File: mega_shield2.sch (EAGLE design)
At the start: 36 parts, among them IC1 L298, IC2 LM2937ET-5V, J2 Mega R3

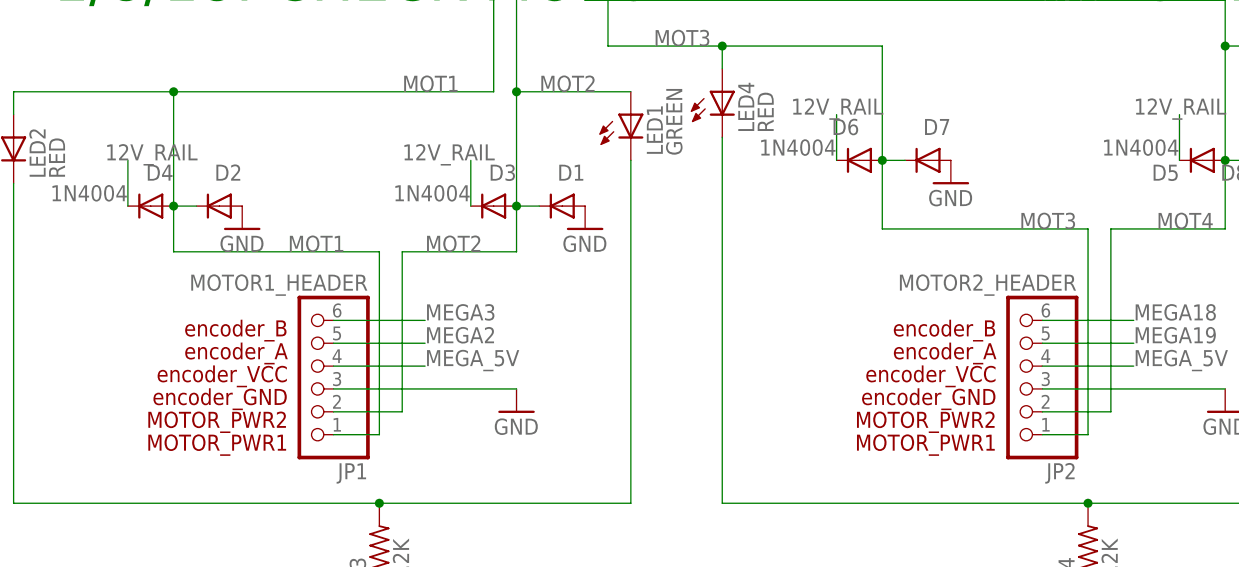
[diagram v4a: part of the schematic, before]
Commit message: changes to silkscreen
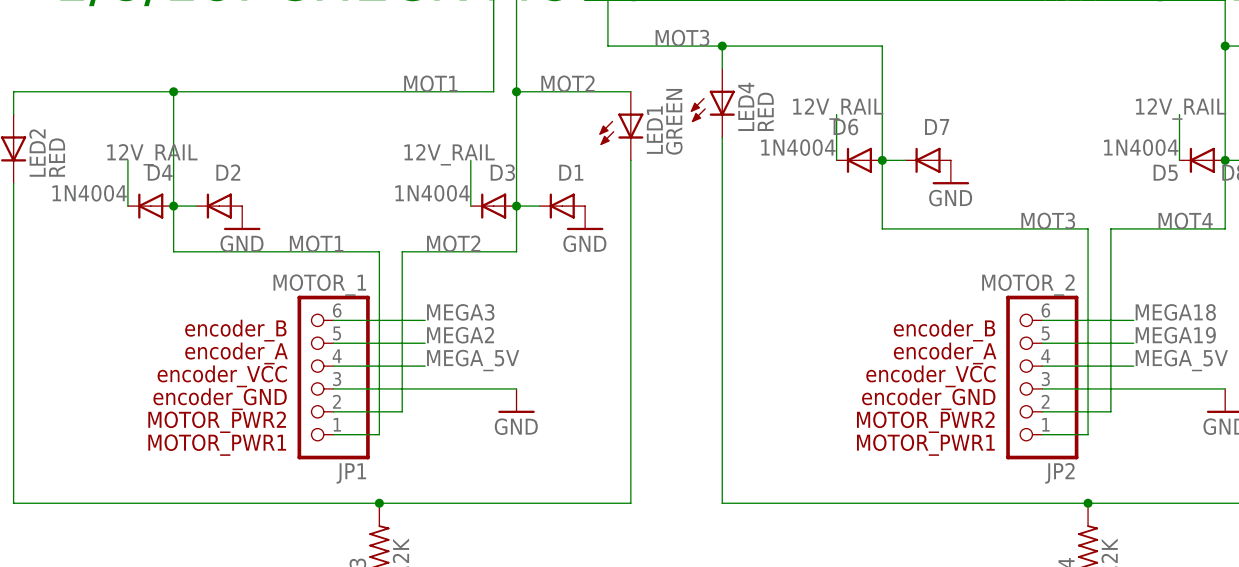
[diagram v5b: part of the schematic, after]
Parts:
- JP1: value MOTOR1_HEADER -> MOTOR_1
- JP2: value MOTOR2_HEADER -> MOTOR_2
- renumbered U$1 to MPR121, U$2 to SLIDE_SW
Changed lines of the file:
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@@
 <part name="12V_IN" library="adafruit" deviceset="1X2" device="-3.5MM"/>
 <part name="GND2" library="supply1" deviceset="GND" device=""/>
-<part name="U$1" library="arduinoShield" deviceset="ADA_MPR121" device=""/>
+<part name="MPR121" library="arduinoShield" deviceset="ADA_MPR121" device=""/>
 <part name="C4" library="rcl" deviceset="C-US" device="025-050X050" value="0.1 uF"/>
 <part name="GND3" library="supply1" deviceset="GND" device=""/>
 <part name="GND13" library="supply1" deviceset="GND" device=""/>
-<part name="JP1" library="adafruit" deviceset="PINHD-1X6" device="" value="MOTOR1_HEADER"/>
+<part name="JP1" library="adafruit" deviceset="PINHD-1X6" device="" value="MOTOR_1"/>
 <part name="GND14" library="supply1" deviceset="GND" device=""/>
-<part name="JP2" library="adafruit" deviceset="PINHD-1X6" device="" value="MOTOR2_HEADER"/>
+<part name="JP2" library="adafruit" deviceset="PINHD-1X6" device="" value="MOTOR_2"/>
 <part name="GND15" library="supply1" deviceset="GND" device=""/>
-<part name="U$2" library="arduinoShield" deviceset="E-SWITCH_500SSP1S2M2QEA" device=""/>
+<part name="SLIDE_SW" library="arduinoShield" deviceset="E-SWITCH_500SSP1S2M2QEA" device=""/>
 </parts>
 <sheets>
@@
 <instance part="12V_IN" gate="G$1" x="15.24" y="-20.32" rot="R90"/>
 <instance part="GND2" gate="1" x="22.86" y="-27.94"/>
-<instance part="U$1" gate="G$1" x="-45.72" y="25.4"/>
+<instance part="MPR121" gate="G$1" x="-45.72" y="25.4"/>
 <instance part="C4" gate="G$1" x="-2.54" y="11.43"/>
 <instance part="GND3" gate="1" x="-2.54" y="3.81"/>
@@
 <instance part="JP2" gate="A" x="48.26" y="-137.16" rot="R180"/>
 <instance part="GND15" gate="1" x="71.12" y="-142.24"/>
-<instance part="U$2" gate="G$1" x="1.778" y="-46.482" rot="R90"/>
+<instance part="SLIDE_SW" gate="G$1" x="1.778" y="-46.482" rot="R90"/>
 </instances>
 <busses>
@@
 <pinref part="C4" gate="G$1" pin="2"/>
 <pinref part="GND3" gate="1" pin="GND"/>
-<pinref part="U$1" gate="G$1" pin="GND2"/>
+<pinref part="MPR121" gate="G$1" pin="GND2"/>
 <wire x1="-15.24" y1="6.35" x2="-2.54" y2="6.35" width="0.1524" layer="91"/>
 <junction x="-2.54" y="6.35"/>
 </segment>
 <segment>
-<pinref part="U$1" gate="G$1" pin="GND"/>
+<pinref part="MPR121" gate="G$1" pin="GND"/>
 <pinref part="GND13" gate="1" pin="GND"/>
 <wire x1="-45.72" y1="25.4" x2="-50.8" y2="25.4" width="0.1524" layer="91"/>
@@
 <pinref part="IMU1" gate="G$1" pin="SDA"/>
 <wire x1="-5.08" y1="40.64" x2="0" y2="40.64" width="0.1524" layer="91"/>
-<pinref part="U$1" gate="G$1" pin="SDA"/>
+<pinref part="MPR121" gate="G$1" pin="SDA"/>
 <wire x1="-15.24" y1="-1.27" x2="-10.16" y2="-1.27" width="0.1524" layer="91"/>
 <wire x1="-10.16" y1="-1.27" x2="-10.16" y2="38.1" width="0.1524" layer="91"/>
@@
 <pinref part="IMU1" gate="G$1" pin="SCL"/>
 <label x="-78.74" y="35.56" size="1.778" layer="95"/>
-<pinref part="U$1" gate="G$1" pin="SCL"/>
+<pinref part="MPR121" gate="G$1" pin="SCL"/>
 <wire x1="-7.62" y1="35.56" x2="0" y2="35.56" width="0.1524" layer="91"/>
 <wire x1="-15.24" y1="-5.08" x2="-7.62" y2="-5.08" width="0.1524" layer="91"/>
@@
 </segment>
 <segment>
-<pinref part="U$1" gate="G$1" pin="VIN"/>
+<pinref part="MPR121" gate="G$1" pin="VIN"/>
 <pinref part="C4" gate="G$1" pin="1"/>
 <wire x1="-15.24" y1="13.97" x2="-2.54" y2="13.97" width="0.1524" layer="91"/>
@@
 <wire x1="-12.7" y1="-53.34" x2="7.62" y2="-53.34" width="0.1524" layer="91"/>
 <label x="-7.62" y="-50.8" size="1.778" layer="95"/>
-<pinref part="U$2" gate="G$1" pin="COM"/>
+<pinref part="SLIDE_SW" gate="G$1" pin="COM"/>
 <wire x1="7.62" y1="-44.958" x2="7.62" y2="-53.34" width="0.1524" layer="91"/>
 <junction x="7.62" y="-53.34"/>
@@
 <pinref part="12V_IN" gate="G$1" pin="1"/>
 <wire x1="5.08" y1="-25.4" x2="12.7" y2="-25.4" width="0.1524" layer="91"/>
-<pinref part="U$2" gate="G$1" pin="L1"/>
+<pinref part="SLIDE_SW" gate="G$1" pin="L1"/>
 <wire x1="4.826" y1="-29.21" x2="5.08" y2="-29.21" width="0.1524" layer="91"/>
 <wire x1="5.08" y1="-29.21" x2="5.08" y2="-25.4" width="0.1524" layer="91"/>

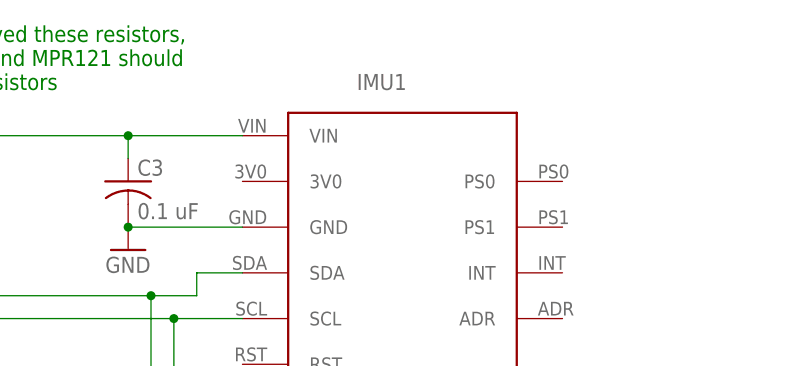
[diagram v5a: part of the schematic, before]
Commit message: shifted some components around, edited silkscreen
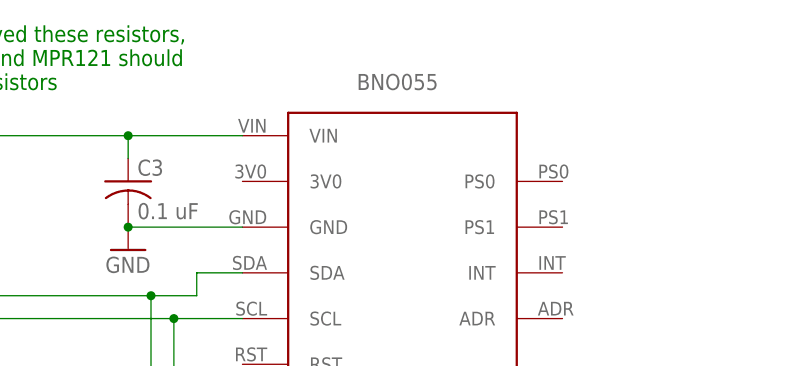
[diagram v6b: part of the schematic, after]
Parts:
- renumbered IMU1 to BNO055
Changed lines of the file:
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@@
 <part name="GND37" library="supply1" deviceset="GND" device=""/>
 <part name="GND20" library="supply1" deviceset="GND" device=""/>
-<part name="IMU1" library="arduinoShield" deviceset="BNO055" device=""/>
+<part name="BNO055" library="arduinoShield" deviceset="BNO055" device=""/>
 <part name="R5" library="rcl" deviceset="R-US_" device="0207/10" value="1K"/>
 <part name="R6" library="rcl" deviceset="R-US_" device="0207/10" value="1K"/>
@@
 <instance part="GND37" gate="1" x="-157.48" y="53.34" rot="R180"/>
 <instance part="GND20" gate="1" x="-66.04" y="53.34" rot="MR0"/>
-<instance part="IMU1" gate="G$1" x="0" y="60.96"/>
+<instance part="BNO055" gate="G$1" x="0" y="60.96"/>
 <instance part="R5" gate="G$1" x="-152.4" y="-7.62"/>
 <instance part="R6" gate="G$1" x="-149.86" y="-12.7"/>
@@
 </segment>
 <segment>
-<pinref part="IMU1" gate="G$1" pin="GND"/>
+<pinref part="BNO055" gate="G$1" pin="GND"/>
 <pinref part="GND1" gate="1" pin="GND"/>
 <pinref part="C3" gate="G$1" pin="2"/>
@@
 <wire x1="-10.16" y1="38.1" x2="-5.08" y2="38.1" width="0.1524" layer="91"/>
 <wire x1="-5.08" y1="38.1" x2="-5.08" y2="40.64" width="0.1524" layer="91"/>
-<pinref part="IMU1" gate="G$1" pin="SDA"/>
+<pinref part="BNO055" gate="G$1" pin="SDA"/>
 <wire x1="-5.08" y1="40.64" x2="0" y2="40.64" width="0.1524" layer="91"/>
 <pinref part="MPR121" gate="G$1" pin="SDA"/>
@@
 <net name="MEGASCL" class="0">
 <segment>
-<pinref part="IMU1" gate="G$1" pin="SCL"/>
+<pinref part="BNO055" gate="G$1" pin="SCL"/>
 <label x="-78.74" y="35.56" size="1.778" layer="95"/>
 <pinref part="MPR121" gate="G$1" pin="SCL"/>
@@
 <net name="MEGA_5V" class="2">
 <segment>
-<pinref part="IMU1" gate="G$1" pin="VIN"/>
+<pinref part="BNO055" gate="G$1" pin="VIN"/>
 <label x="-43.18" y="55.88" size="1.778" layer="95"/>
 <pinref part="C3" gate="G$1" pin="1"/>
@@
 </segment>
 </net>
-<net name="MOT4" class="2">
+<net name="MOT4" class="1">
 <segment>
 <pinref part="D8" gate="1" pin="C"/>
